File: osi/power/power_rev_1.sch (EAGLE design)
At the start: 11 parts

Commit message: update
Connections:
- removed net D8: JP5.5
- new net D10: JP5.6
- net D9: now also JP5.5; no longer JP5.6
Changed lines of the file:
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@@
 <wire x1="119.38" y1="40.64" x2="114.3" y2="40.64" width="0.1524" layer="91"/>
 <pinref part="JP6" gate="G$1" pin="5"/>
+<label x="114.3" y="40.64" size="1.778" layer="95"/>
 </segment>
 </net>
@@
 <wire x1="119.38" y1="38.1" x2="114.3" y2="38.1" width="0.1524" layer="91"/>
 <pinref part="JP6" gate="G$1" pin="6"/>
+<label x="114.3" y="38.1" size="1.778" layer="95"/>
 </segment>
 </net>
@@
 <wire x1="119.38" y1="35.56" x2="114.3" y2="35.56" width="0.1524" layer="91"/>
 <pinref part="JP6" gate="G$1" pin="7"/>
+<label x="114.3" y="35.56" size="1.778" layer="95"/>
 </segment>
 </net>
@@
 <wire x1="119.38" y1="33.02" x2="114.3" y2="33.02" width="0.1524" layer="91"/>
 <pinref part="JP6" gate="G$1" pin="8"/>
+<label x="105.918" y="33.274" size="1.778" layer="95"/>
 </segment>
 </net>
@@
 <wire x1="114.3" y1="48.26" x2="119.38" y2="48.26" width="0.1524" layer="91"/>
 <pinref part="JP6" gate="G$1" pin="2"/>
+<label x="107.696" y="48.26" size="1.778" layer="95"/>
 </segment>
 </net>
@@
 <wire x1="114.3" y1="45.72" x2="119.38" y2="45.72" width="0.1524" layer="91"/>
 <pinref part="JP6" gate="G$1" pin="3"/>
+<label x="114.3" y="45.72" size="1.778" layer="95"/>
 </segment>
 </net>
@@
 <wire x1="114.3" y1="43.18" x2="119.38" y2="43.18" width="0.1524" layer="91"/>
 <pinref part="JP6" gate="G$1" pin="4"/>
-</segment>
-</net>
-<net name="D8" class="0">
-<segment>
-<wire x1="114.3" y1="60.96" x2="119.38" y2="60.96" width="0.1524" layer="91"/>
-<pinref part="JP5" gate="G$1" pin="5"/>
+<label x="107.95" y="43.434" size="1.778" layer="95"/>
 </segment>
 </net>
 <net name="D9" class="0">
 <segment>
-<wire x1="114.3" y1="58.42" x2="119.38" y2="58.42" width="0.1524" layer="91"/>
-<pinref part="JP5" gate="G$1" pin="6"/>
+<wire x1="114.3" y1="60.96" x2="119.38" y2="60.96" width="0.1524" layer="91"/>
+<pinref part="JP5" gate="G$1" pin="5"/>
+<label x="114.3" y="60.96" size="1.778" layer="95"/>
 </segment>
 </net>
 <net name="D10" class="0">
 <segment>
-<wire x1="114.3" y1="55.88" x2="132.08" y2="55.88" width="0.1524" layer="91"/>
+<wire x1="114.3" y1="58.42" x2="119.38" y2="58.42" width="0.1524" layer="91"/>
+<pinref part="JP5" gate="G$1" pin="6"/>
+<label x="114.3" y="58.42" size="1.778" layer="95"/>
 </segment>
 </net>
@@
 <wire x1="114.3" y1="50.8" x2="119.38" y2="50.8" width="0.1524" layer="91"/>
 <pinref part="JP6" gate="G$1" pin="1"/>
+<label x="114.3" y="50.8" size="1.778" layer="95"/>
 </segment>
 </net>

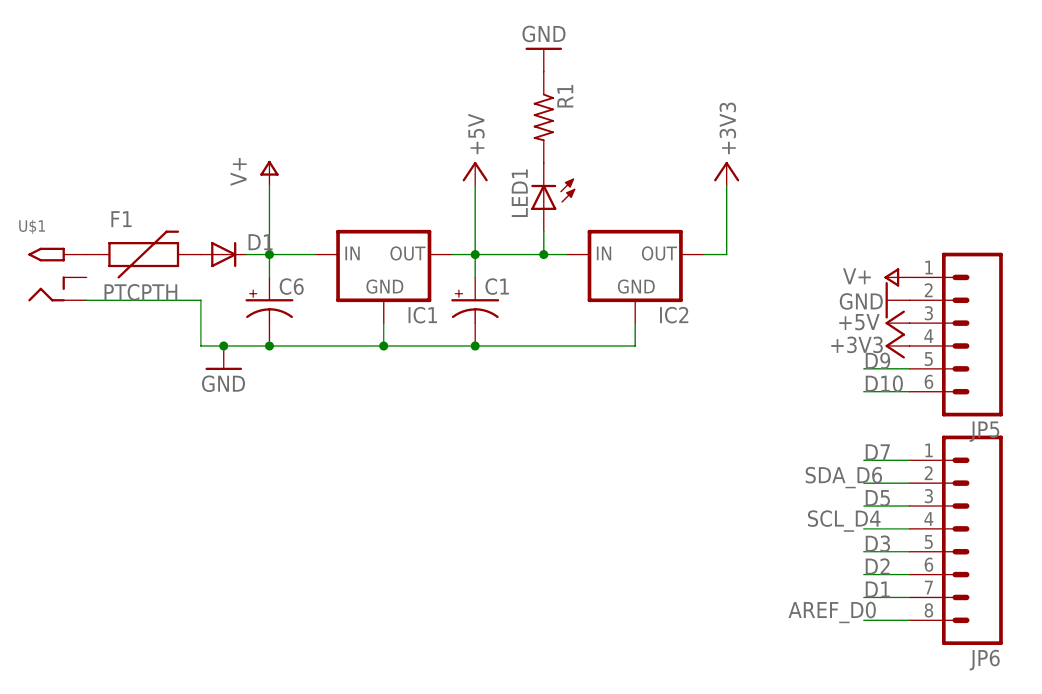
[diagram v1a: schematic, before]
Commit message: D9 -> D8 for INT0
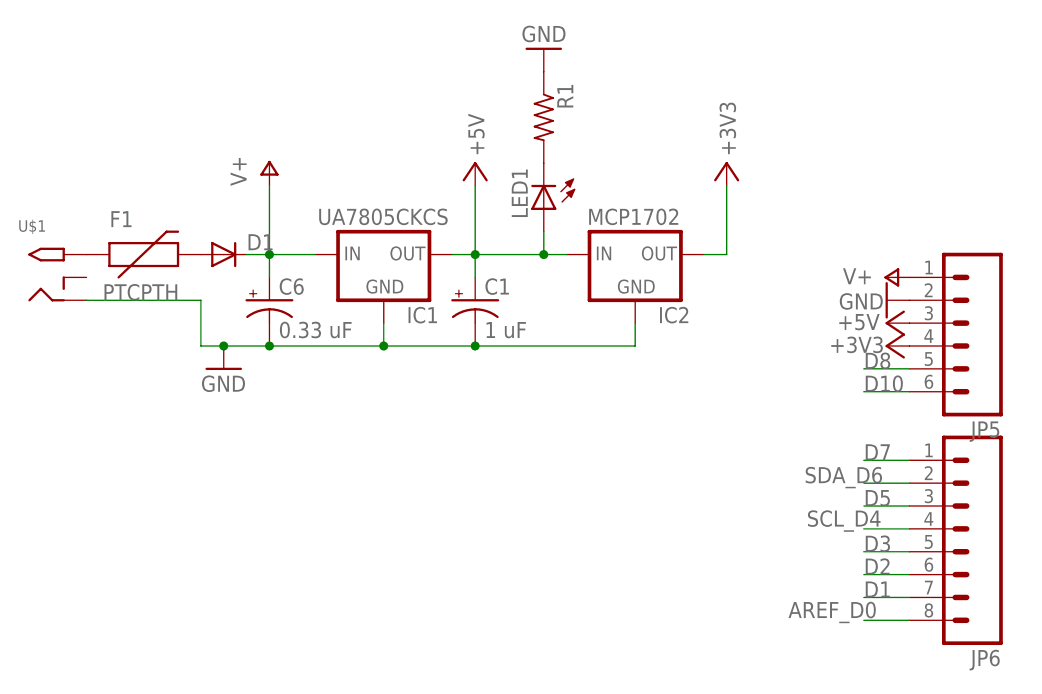
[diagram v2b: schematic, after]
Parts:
- C1: value (none) -> 1 uF
- C6: value (none) -> 0.33 uF
- IC1: value (none) -> UA7805CKCS
- IC2: value (none) -> MCP1702
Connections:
- net D9 renamed D8
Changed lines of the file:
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@@
 <part name="JP6" library="SparkFun" deviceset="M08" device="1X08"/>
 <part name="U$1" library="adafruit" deviceset="2.1MMJACK" device="THM"/>
-<part name="IC1" library="SparkFun" deviceset="V_REG_78XX" device="-TO-220"/>
+<part name="IC1" library="SparkFun" deviceset="V_REG_78XX" device="-TO-220" value="UA7805CKCS"/>
 <part name="D1" library="SparkFun" deviceset="DIODE" device="1N4148"/>
-<part name="IC2" library="adafruit" deviceset="MCP1700" device="INLINE"/>
-<part name="C6" library="SparkFun" deviceset="CAP_POL" device="PTH1"/>
-<part name="C1" library="SparkFun" deviceset="CAP_POL" device="PTH1"/>
+<part name="IC2" library="adafruit" deviceset="MCP1700" device="INLINE" value="MCP1702"/>
+<part name="C6" library="SparkFun" deviceset="CAP_POL" device="PTH1" value="0.33 uF"/>
+<part name="C1" library="SparkFun" deviceset="CAP_POL" device="PTH1" value="1 uF"/>
 <part name="LED1" library="adafruit" deviceset="LED" device="3MM"/>
 <part name="R1" library="adafruit" deviceset="R-US_" device="0204/2V"/>
 <part name="GND1" library="SparkFun" deviceset="GND" device=""/>
 <part name="F1" library="SparkFun_mod" deviceset="PTC" device="PTH"/>
+<part name="FRAME1" library="SparkFun_mod" deviceset="FRAME-LETTER" device=""/>
 </parts>
 <sheets>
@@
 <instance part="JP6" gate="G$1" x="124.46" y="43.18" rot="R180"/>
 <instance part="U$1" gate="G$1" x="22.86" y="71.12"/>
-<instance part="IC1" gate="G$1" x="60.96" y="73.66"/>
+<instance part="IC1" gate="G$1" x="60.96" y="73.66" smashed="yes">
+<attribute name="NAME" x="63.5" y="66.04" size="1.778" layer="95"/>
+<attribute name="VALUE" x="53.594" y="76.962" size="1.778" layer="96"/>
+</instance>
 <instance part="D1" gate="G$1" x="43.18" y="73.66"/>
-<instance part="IC2" gate="1" x="88.9" y="73.66"/>
+<instance part="IC2" gate="1" x="88.9" y="73.66" smashed="yes">
+<attribute name="NAME" x="91.44" y="66.04" size="1.778" layer="95"/>
+<attribute name="VALUE" x="83.566" y="76.962" size="1.778" layer="96"/>
+</instance>
 <instance part="C6" gate="G$1" x="48.26" y="68.58"/>
 <instance part="C1" gate="G$1" x="71.12" y="68.58"/>
@@
 <instance part="GND1" gate="1" x="78.74" y="96.52" rot="R180"/>
 <instance part="F1" gate="G$1" x="33.02" y="73.66"/>
+<instance part="FRAME1" gate="G$1" x="-63.5" y="-38.1"/>
+<instance part="FRAME1" gate="G$2" x="83.82" y="-38.1"/>
 </instances>
 <busses>
@@
 </segment>
 </net>
-<net name="D9" class="0">
+<net name="D8" class="0">
 <segment>
 <wire x1="114.3" y1="60.96" x2="119.38" y2="60.96" width="0.1524" layer="91"/>
